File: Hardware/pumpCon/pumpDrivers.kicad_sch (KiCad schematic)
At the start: 50 parts, among them J10 Conn_01x02, J11 Conn_01x02, J12 Conn_01x05, J13 Conn_01x05, J14 Conn_01x05, J15 Conn_01x05, J16 Conn_01x05, J17 Conn_01x05, J18 Conn_01x05, J19 Conn_01x05, U10 74HC595, U11 ULN2003F12, U12 ULN2003F12, U13 ULN2003F12, U14 ULN2003F12, U15 74HC595, U16 74HC595, U17 ULN2003F12, U18 ULN2003F12, U19 ULN2003F12, U20 ULN2003F12, U7 DRV8231ADSGR, U8 DRV8231ADSGR, U9 74HC595

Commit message: wip
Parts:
- L6, L7: value 33µ -> 100u
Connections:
- net GND: no longer C39.1, C40.1, C41.2, C42.2
- net at J11.2 (Pin_2), U8.8 (OUT2): now also C40.1, C42.2
- net at J10.2 (Pin_2), U7.8 (OUT2): now also C39.1, C41.2
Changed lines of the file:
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@@
 (kicad_sch (version 20211123) (generator eeschema)
   (paper "A4")
+  (junction (at 93.98 113.03) (diameter 0) (color 0 0 0 0)
+  )
   (junction (at 261.62 80.01) (diameter 0) (color 0 0 0 0)
   )
@@
   (junction (at 275.59 133.35) (diameter 0) (color 0 0 0 0)
   )
+  (junction (at 95.25 171.45) (diameter 0) (color 0 0 0 0)
+  )
   (junction (at 261.62 153.67) (diameter 0) (color 0 0 0 0)
   )
   (junction (at 275.59 59.69) (diameter 0) (color 0 0 0 0)
   )
+  (junction (at 88.9 101.6) (diameter 0) (color 0 0 0 0)
+  )
   (junction (at 177.8 153.67) (diameter 0) (color 0 0 0 0)
   )
@@
   (junction (at 95.25 157.48) (diameter 0) (color 0 0 0 0)
   )
+  (junction (at 91.44 160.02) (diameter 0) (color 0 0 0 0)
+  )
   (junction (at 191.77 25.4) (diameter 0) (color 0 0 0 0)
   )
@@
     (stroke (width 0) (type default) (color 0 0 0 0))
   )
+  (wire (pts (xy 88.9 101.6) (xy 80.01 101.6))
+    (stroke (width 0) (type default) (color 0 0 0 0))
+  )
   (wire (pts (xy 247.65 140.97) (xy 247.65 127))
     (stroke (width 0) (type default) (color 0 0 0 0))
@@
     (stroke (width 0) (type default) (color 0 0 0 0))
   )
+  (wire (pts (xy 93.98 113.03) (xy 88.9 113.03))
+    (stroke (width 0) (type default) (color 0 0 0 0))
+  )
   (wire (pts (xy 80.01 113.03) (xy 81.28 113.03))
     (stroke (width 0) (type default) (color 0 0 0 0))
@@
     (stroke (width 0) (type default) (color 0 0 0 0))
   )
+  (wire (pts (xy 95.25 171.45) (xy 91.44 171.45))
+    (stroke (width 0) (type default) (color 0 0 0 0))
+  )
   (wire (pts (xy 58.42 115.57) (xy 59.69 115.57))
     (stroke (width 0) (type default) (color 0 0 0 0))
@@
     (stroke (width 0) (type default) (color 0 0 0 0))
   )
+  (wire (pts (xy 95.25 171.45) (xy 102.87 171.45))
+    (stroke (width 0) (type default) (color 0 0 0 0))
+  )
   (wire (pts (xy 241.3 55.88) (xy 238.76 55.88))
     (stroke (width 0) (type default) (color 0 0 0 0))
@@
     (stroke (width 0) (type default) (color 0 0 0 0))
   )
-  (wire (pts (xy 81.28 160.02) (xy 104.14 160.02))
+  (wire (pts (xy 81.28 160.02) (xy 91.44 160.02))
     (stroke (width 0) (type default) (color 0 0 0 0))
   )
@@
     (stroke (width 0) (type default) (color 0 0 0 0))
   )
+  (wire (pts (xy 91.44 171.45) (xy 91.44 160.02))
+    (stroke (width 0) (type default) (color 0 0 0 0))
+  )
   (wire (pts (xy 95.25 157.48) (xy 93.98 157.48))
     (stroke (width 0) (type default) (color 0 0 0 0))
@@
     (stroke (width 0) (type default) (color 0 0 0 0))
   )
-  (wire (pts (xy 102.87 101.6) (xy 80.01 101.6))
+  (wire (pts (xy 102.87 101.6) (xy 88.9 101.6))
     (stroke (width 0) (type default) (color 0 0 0 0))
   )
@@
     (stroke (width 0) (type default) (color 0 0 0 0))
   )
+  (wire (pts (xy 101.6 113.03) (xy 93.98 113.03))
+    (stroke (width 0) (type default) (color 0 0 0 0))
+  )
   (wire (pts (xy 95.25 163.83) (xy 95.25 157.48))
     (stroke (width 0) (type default) (color 0 0 0 0))
@@
     (stroke (width 0) (type default) (color 0 0 0 0))
   )
+  (wire (pts (xy 88.9 113.03) (xy 88.9 101.6))
+    (stroke (width 0) (type default) (color 0 0 0 0))
+  )
   (wire (pts (xy 158.75 30.48) (xy 168.91 30.48))
     (stroke (width 0) (type default) (color 0 0 0 0))
@@
   )
   (wire (pts (xy 163.83 67.31) (xy 163.83 50.8))
+    (stroke (width 0) (type default) (color 0 0 0 0))
+  )
+  (wire (pts (xy 91.44 160.02) (xy 104.14 160.02))
     (stroke (width 0) (type default) (color 0 0 0 0))
   )
@@
     (pin "2")
   )
-  (symbol (lib_id "power:GND") (at 93.98 113.03 0) (unit 1)
-    (in_bom yes) (on_board yes)
-    (property "Reference" "#PWR0231" (id 0) (at 93.98 119.38 0)
-      (effects (font (size 1.27 1.27)) hide)
-    )
-    (property "Value" "GND" (id 1) (at 93.98 116.84 0))
-    (property "Footprint" "" (id 2) (at 93.98 113.03 0)
-      (effects (font (size 1.27 1.27)) hide)
-    )
-    (property "Datasheet" "" (id 3) (at 93.98 113.03 0)
-      (effects (font (size 1.27 1.27)) hide)
-    )
-    (pin "1")
-  )
   (symbol (lib_id "power:GND") (at 59.69 182.88 0) (unit 1)
     (in_bom yes) (on_board yes)
@@
     (pin "1")
   )
-  (symbol (lib_id "power:GND") (at 95.25 171.45 0) (unit 1)
-    (in_bom yes) (on_board yes)
-    (property "Reference" "#PWR0227" (id 0) (at 95.25 177.8 0)
-      (effects (font (size 1.27 1.27)) hide)
-    )
-    (property "Value" "GND" (id 1) (at 95.25 175.26 0))
-    (property "Footprint" "" (id 2) (at 95.25 171.45 0)
-      (effects (font (size 1.27 1.27)) hide)
-    )
-    (property "Datasheet" "" (id 3) (at 95.25 171.45 0)
-      (effects (font (size 1.27 1.27)) hide)
-    )
-    (pin "1")
-  )
   (symbol (lib_id "Connector_Generic:Conn_01x05") (at 196.85 105.41 0) (unit 1)
     (in_bom yes) (on_board yes)
@@
     (pin "9")
   )
-  (symbol (lib_id "power:GND") (at 101.6 113.03 0) (unit 1)
-    (in_bom yes) (on_board yes)
-    (property "Reference" "#PWR0230" (id 0) (at 101.6 119.38 0)
-      (effects (font (size 1.27 1.27)) hide)
-    )
-    (property "Value" "GND" (id 1) (at 101.6 116.84 0))
-    (property "Footprint" "" (id 2) (at 101.6 113.03 0)
-      (effects (font (size 1.27 1.27)) hide)
-    )
-    (property "Datasheet" "" (id 3) (at 101.6 113.03 0)
-      (effects (font (size 1.27 1.27)) hide)
-    )
-    (pin "1")
-  )
   (symbol (lib_id "Bergi:DRV8231ADSGR") (at 71.12 157.48 0) (unit 1)
     (in_bom yes) (on_board yes) (fields_autoplaced)
@@
     (in_bom yes) (on_board yes) (fields_autoplaced)
     (property "Reference" "L7" (id 0) (at 90.17 151.13 90))
-    (property "Value" "33µ" (id 1) (at 90.17 153.67 90))
+    (property "Value" "100u" (id 1) (at 90.17 153.67 90))
     (property "Footprint" "Inductor_SMD:L_12x12mm_H8mm" (id 2) (at 90.17 157.48 0)
       (effects (font (size 1.27 1.27)) hide)
@@
     (in_bom yes) (on_board yes) (fields_autoplaced)
     (property "Reference" "L6" (id 0) (at 88.9 92.71 90))
-    (property "Value" "33µ" (id 1) (at 88.9 95.25 90))
+    (property "Value" "100u" (id 1) (at 88.9 95.25 90))
     (property "Footprint" "Inductor_SMD:L_12x12mm_H8mm" (id 2) (at 88.9 99.06 0)
       (effects (font (size 1.27 1.27)) hide)
@@
       (effects (font (size 1.27 1.27)) hide)
     )
-    (pin "1")
-  )
-  (symbol (lib_id "power:GND") (at 102.87 171.45 0) (unit 1)
-    (in_bom yes) (on_board yes)
-    (property "Reference" "#PWR0228" (id 0) (at 102.87 177.8 0)
-      (effects (font (size 1.27 1.27)) hide)
-    )
-    (property "Value" "GND" (id 1) (at 102.87 175.26 0))
-    (property "Footprint" "" (id 2) (at 102.87 171.45 0)
-      (effects (font (size 1.27 1.27)) hide)
-    )
-    (property "Datasheet" "" (id 3) (at 102.87 171.45 0)
-      (effects (font (size 1.27 1.27)) hide)
-    )

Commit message: pumpCon fully work now
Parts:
- removed C41, C42: 100µ, Capacitor_THT:CP_Radial_D6.3mm_P2.50mm, symbol Device:C_Polarized
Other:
- moved on the sheet: J10, J11
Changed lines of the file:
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@@
 (kicad_sch (version 20211123) (generator eeschema)
   (paper "A4")
-  (junction (at 93.98 113.03) (diameter 0) (color 0 0 0 0)
-  )
   (junction (at 261.62 80.01) (diameter 0) (color 0 0 0 0)
   )
@@
   (junction (at 275.59 133.35) (diameter 0) (color 0 0 0 0)
   )
-  (junction (at 95.25 171.45) (diameter 0) (color 0 0 0 0)
-  )
   (junction (at 261.62 153.67) (diameter 0) (color 0 0 0 0)
   )
@@
   (junction (at 177.8 153.67) (diameter 0) (color 0 0 0 0)
   )
-  (junction (at 101.6 99.06) (diameter 0) (color 0 0 0 0)
-  )
   (junction (at 177.8 45.72) (diameter 0) (color 0 0 0 0)
   )
@@
   (junction (at 59.69 173.99) (diameter 0) (color 0 0 0 0)
   )
-  (junction (at 102.87 157.48) (diameter 0) (color 0 0 0 0)
-  )
   (junction (at 275.59 95.25) (diameter 0) (color 0 0 0 0)
   )
@@
     (stroke (width 0) (type default) (color 0 0 0 0))
   )
-  (wire (pts (xy 102.87 157.48) (xy 104.14 157.48))
-    (stroke (width 0) (type default) (color 0 0 0 0))
-  )
   (wire (pts (xy 158.75 72.39) (xy 158.75 55.88))
     (stroke (width 0) (type default) (color 0 0 0 0))
@@
     (stroke (width 0) (type default) (color 0 0 0 0))
   )
-  (wire (pts (xy 93.98 99.06) (xy 101.6 99.06))
+  (wire (pts (xy 93.98 99.06) (xy 96.52 99.06))
     (stroke (width 0) (type default) (color 0 0 0 0))
   )
@@
     (stroke (width 0) (type default) (color 0 0 0 0))
   )
-  (wire (pts (xy 102.87 163.83) (xy 102.87 157.48))
-    (stroke (width 0) (type default) (color 0 0 0 0))
-  )
   (wire (pts (xy 177.8 45.72) (xy 180.34 45.72))
     (stroke (width 0) (type default) (color 0 0 0 0))
@@
     (stroke (width 0) (type default) (color 0 0 0 0))
   )
-  (wire (pts (xy 95.25 171.45) (xy 102.87 171.45))
-    (stroke (width 0) (type default) (color 0 0 0 0))
-  )
   (wire (pts (xy 241.3 55.88) (xy 238.76 55.88))
     (stroke (width 0) (type default) (color 0 0 0 0))
@@
     (stroke (width 0) (type default) (color 0 0 0 0))
   )
-  (wire (pts (xy 102.87 101.6) (xy 88.9 101.6))
+  (wire (pts (xy 96.52 101.6) (xy 88.9 101.6))
     (stroke (width 0) (type default) (color 0 0 0 0))
   )
@@
     (stroke (width 0) (type default) (color 0 0 0 0))
   )
-  (wire (pts (xy 101.6 113.03) (xy 93.98 113.03))
-    (stroke (width 0) (type default) (color 0 0 0 0))
-  )
   (wire (pts (xy 95.25 163.83) (xy 95.25 157.48))
     (stroke (width 0) (type default) (color 0 0 0 0))
@@
     (stroke (width 0) (type default) (color 0 0 0 0))
   )
-  (wire (pts (xy 95.25 157.48) (xy 102.87 157.48))
+  (wire (pts (xy 95.25 157.48) (xy 97.79 157.48))
     (stroke (width 0) (type default) (color 0 0 0 0))
   )
@@
     (stroke (width 0) (type default) (color 0 0 0 0))
   )
-  (wire (pts (xy 91.44 160.02) (xy 104.14 160.02))
+  (wire (pts (xy 91.44 160.02) (xy 97.79 160.02))
     (stroke (width 0) (type default) (color 0 0 0 0))
   )
@@
     (stroke (width 0) (type default) (color 0 0 0 0))
   )
-  (wire (pts (xy 101.6 99.06) (xy 102.87 99.06))
-    (stroke (width 0) (type default) (color 0 0 0 0))
-  )
   (wire (pts (xy 242.57 114.3) (xy 242.57 100.33))
     (stroke (width 0) (type default) (color 0 0 0 0))
@@
   )
   (wire (pts (xy 242.57 146.05) (xy 252.73 146.05))
-    (stroke (width 0) (type default) (color 0 0 0 0))
-  )
-  (wire (pts (xy 101.6 105.41) (xy 101.6 99.06))
     (stroke (width 0) (type default) (color 0 0 0 0))
   )
@@
     (pin "1")
   )
-  (symbol (lib_id "Device:C_Polarized") (at 101.6 109.22 0) (unit 1)
-    (in_bom yes) (on_board yes) (fields_autoplaced)
-    (property "Reference" "C41" (id 0) (at 105.41 107.0609 0)
-      (effects (font (size 1.27 1.27)) (justify left))
-    )
-    (property "Value" "100µ" (id 1) (at 105.41 109.6009 0)
-      (effects (font (size 1.27 1.27)) (justify left))
-    )
-    (property "Footprint" "Capacitor_THT:CP_Radial_D6.3mm_P2.50mm" (id 2) (at 102.5652 113.03 0)
-      (effects (font (size 1.27 1.27)) hide)
-    )
-    (property "Datasheet" "~" (id 3) (at 101.6 109.22 0)
-      (effects (font (size 1.27 1.27)) hide)
-    )
-    (pin "1")
-    (pin "2")
-  )
   (symbol (lib_id "Device:C") (at 232.41 86.36 0) (unit 1)
     (in_bom yes) (on_board yes)
@@
     (pin "2")
   )
-  (symbol (lib_id "Connector_Generic:Conn_01x02") (at 109.22 157.48 0) (unit 1)
-    (in_bom yes) (on_board yes)
-    (property "Reference" "J11" (id 0) (at 107.95 154.94 0)
-      (effects (font (size 1.27 1.27)) (justify left))
-    )
-    (property "Value" "Conn_01x02" (id 1) (at 107.95 152.4 0)
-      (effects (font (size 1.27 1.27)) (justify left))
-    )
-    (property "Footprint" "Connector_Molex:Molex_KK-254_AE-6410-02A_1x02_P2.54mm_Vertical" (id 2) (at 109.22 157.48 0)
-      (effects (font (size 1.27 1.27)) hide)
-    )
-    (property "Datasheet" "~" (id 3) (at 109.22 157.48 0)
+  (symbol (lib_id "Connector_Generic:Conn_01x02") (at 102.87 157.48 0) (unit 1)
+    (in_bom yes) (on_board yes)
+    (property "Reference" "J11" (id 0) (at 101.6 154.94 0)
+      (effects (font (size 1.27 1.27)) (justify left))
+    )
+    (property "Value" "Conn_01x02" (id 1) (at 101.6 152.4 0)
+      (effects (font (size 1.27 1.27)) (justify left))
+    )
+    (property "Footprint" "Connector_Molex:Molex_KK-254_AE-6410-02A_1x02_P2.54mm_Vertical" (id 2) (at 102.87 157.48 0)
+      (effects (font (size 1.27 1.27)) hide)
+    )
+    (property "Datasheet" "~" (id 3) (at 102.87 157.48 0)
       (effects (font (size 1.27 1.27)) hide)
     )
@@
     (pin "5")
   )
-  (symbol (lib_id "Device:C_Polarized") (at 102.87 167.64 0) (unit 1)
-    (in_bom yes) (on_board yes) (fields_autoplaced)
-    (property "Reference" "C42" (id 0) (at 106.68 165.4809 0)
-      (effects (font (size 1.27 1.27)) (justify left))
-    )
-    (property "Value" "100µ" (id 1) (at 106.68 168.0209 0)
-      (effects (font (size 1.27 1.27)) (justify left))
-    )
-    (property "Footprint" "Capacitor_THT:CP_Radial_D6.3mm_P2.50mm" (id 2) (at 103.8352 171.45 0)
-      (effects (font (size 1.27 1.27)) hide)
-    )
-    (property "Datasheet" "~" (id 3) (at 102.87 167.64 0)
-      (effects (font (size 1.27 1.27)) hide)
-    )
-    (pin "1")
-    (pin "2")
-  )
   (symbol (lib_id "power:GND") (at 275.59 123.19 0) (unit 1)
     (in_bom yes) (on_board yes)
@@
     (pin "1")
   )
-  (symbol (lib_id "Connector_Generic:Conn_01x02") (at 107.95 99.06 0) (unit 1)
-    (in_bom yes) (on_board yes)
-    (property "Reference" "J10" (id 0) (at 106.68 96.52 0)
-      (effects (font (size 1.27 1.27)) (justify left))
-    )
-    (property "Value" "Conn_01x02" (id 1) (at 106.68 93.98 0)
-      (effects (font (size 1.27 1.27)) (justify left))
-    )
-    (property "Footprint" "Connector_Molex:Molex_KK-254_AE-6410-02A_1x02_P2.54mm_Vertical" (id 2) (at 107.95 99.06 0)
-      (effects (font (size 1.27 1.27)) hide)
-    )
-    (property "Datasheet" "~" (id 3) (at 107.95 99.06 0)
-      (effects (font (size 1.27 1.27)) hide)
-    )
+  (symbol (lib_id "Connector_Generic:Conn_01x02") (at 101.6 99.06 0) (unit 1)
+    (in_bom yes) (on_board yes)
+    (property "Reference" "J10" (id 0) (at 100.33 96.52 0)
+      (effects (font (size 1.27 1.27)) (justify left))
+    )
+    (property "Value" "Conn_01x02" (id 1) (at 100.33 93.98 0)
+      (effects (font (size 1.27 1.27)) (justify left))
+    )
+    (property "Footprint" "Connector_Molex:Molex_KK-254_AE-6410-02A_1x02_P2.54mm_Vertical" (id 2) (at 101.6 99.06 0)
+      (effects (font (size 1.27 1.27)) hide)
+    )
+    (property "Datasheet" "~" (id 3) (at 101.6 99.06 0)
+      (effects (font (size 1.27 1.27)) hide)
+    )

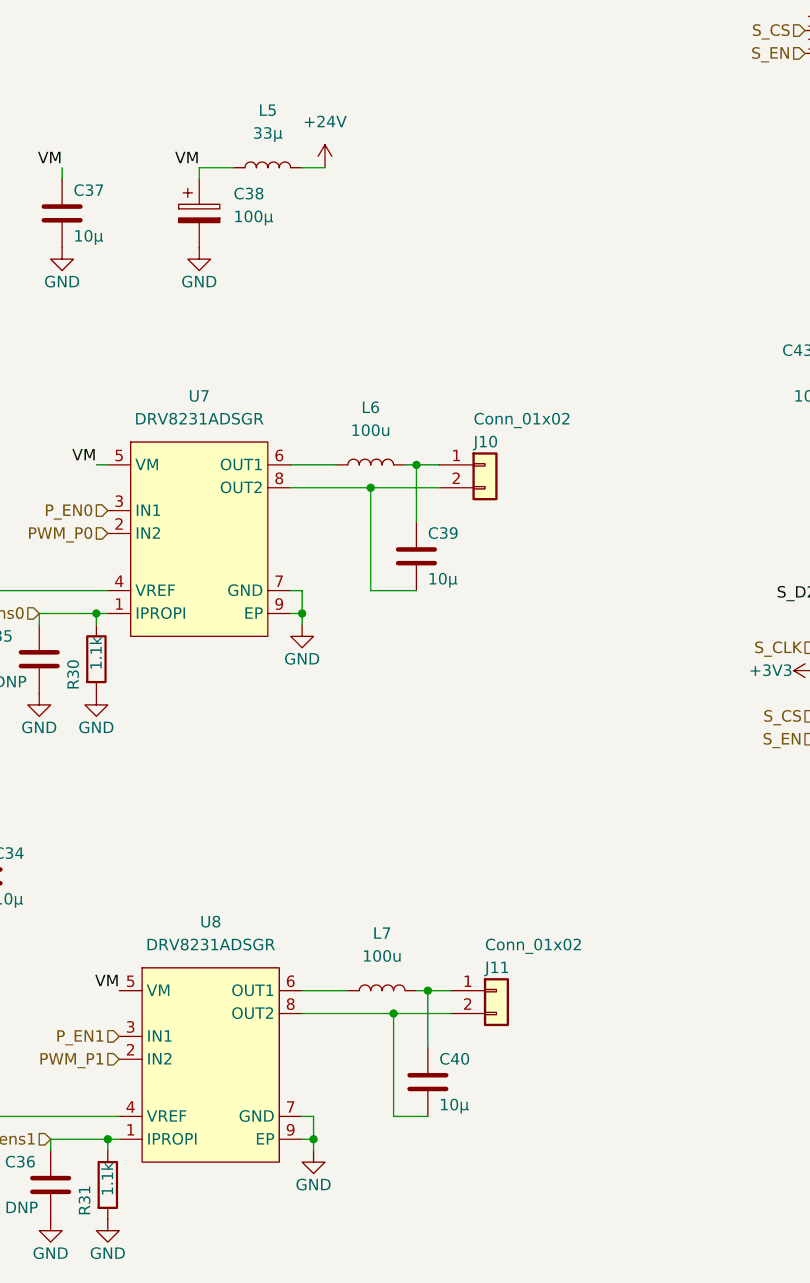
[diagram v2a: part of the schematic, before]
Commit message: modified motor output
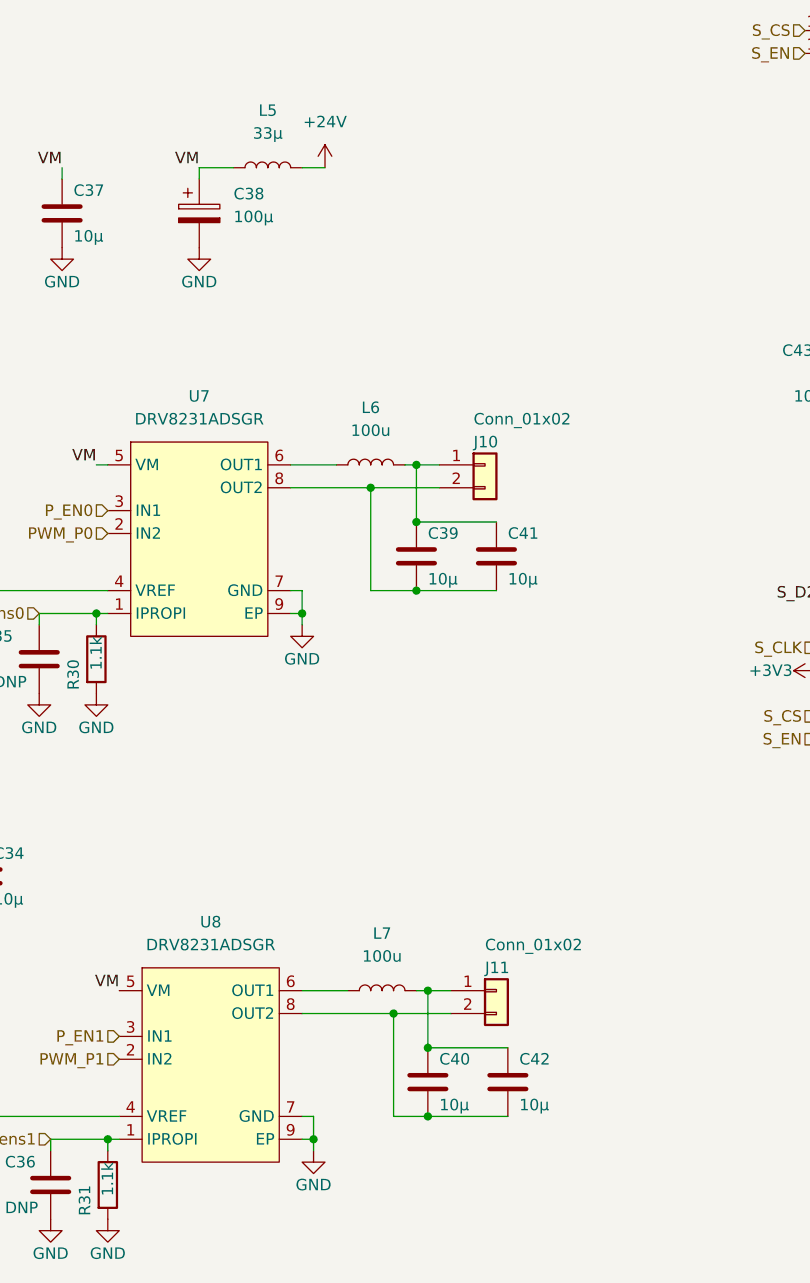
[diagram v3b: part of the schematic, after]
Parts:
- added C41, C42: 10µ, Capacitor_SMD:C_1210_3225Metric, symbol Device:C
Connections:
- net at C40.1, J11.2 (Pin_2), U8.8 (OUT2): now also C42.1
- net at C40.2, J11.1 (Pin_1), L7.2: now also C42.2
- net at C39.1, J10.2 (Pin_2), U7.8 (OUT2): now also C41.1
- net at C39.2, J10.1 (Pin_1), L6.2: now also C41.2
